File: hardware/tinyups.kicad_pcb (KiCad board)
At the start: 4 copper layers, 150 x 140 mm, 30 parts

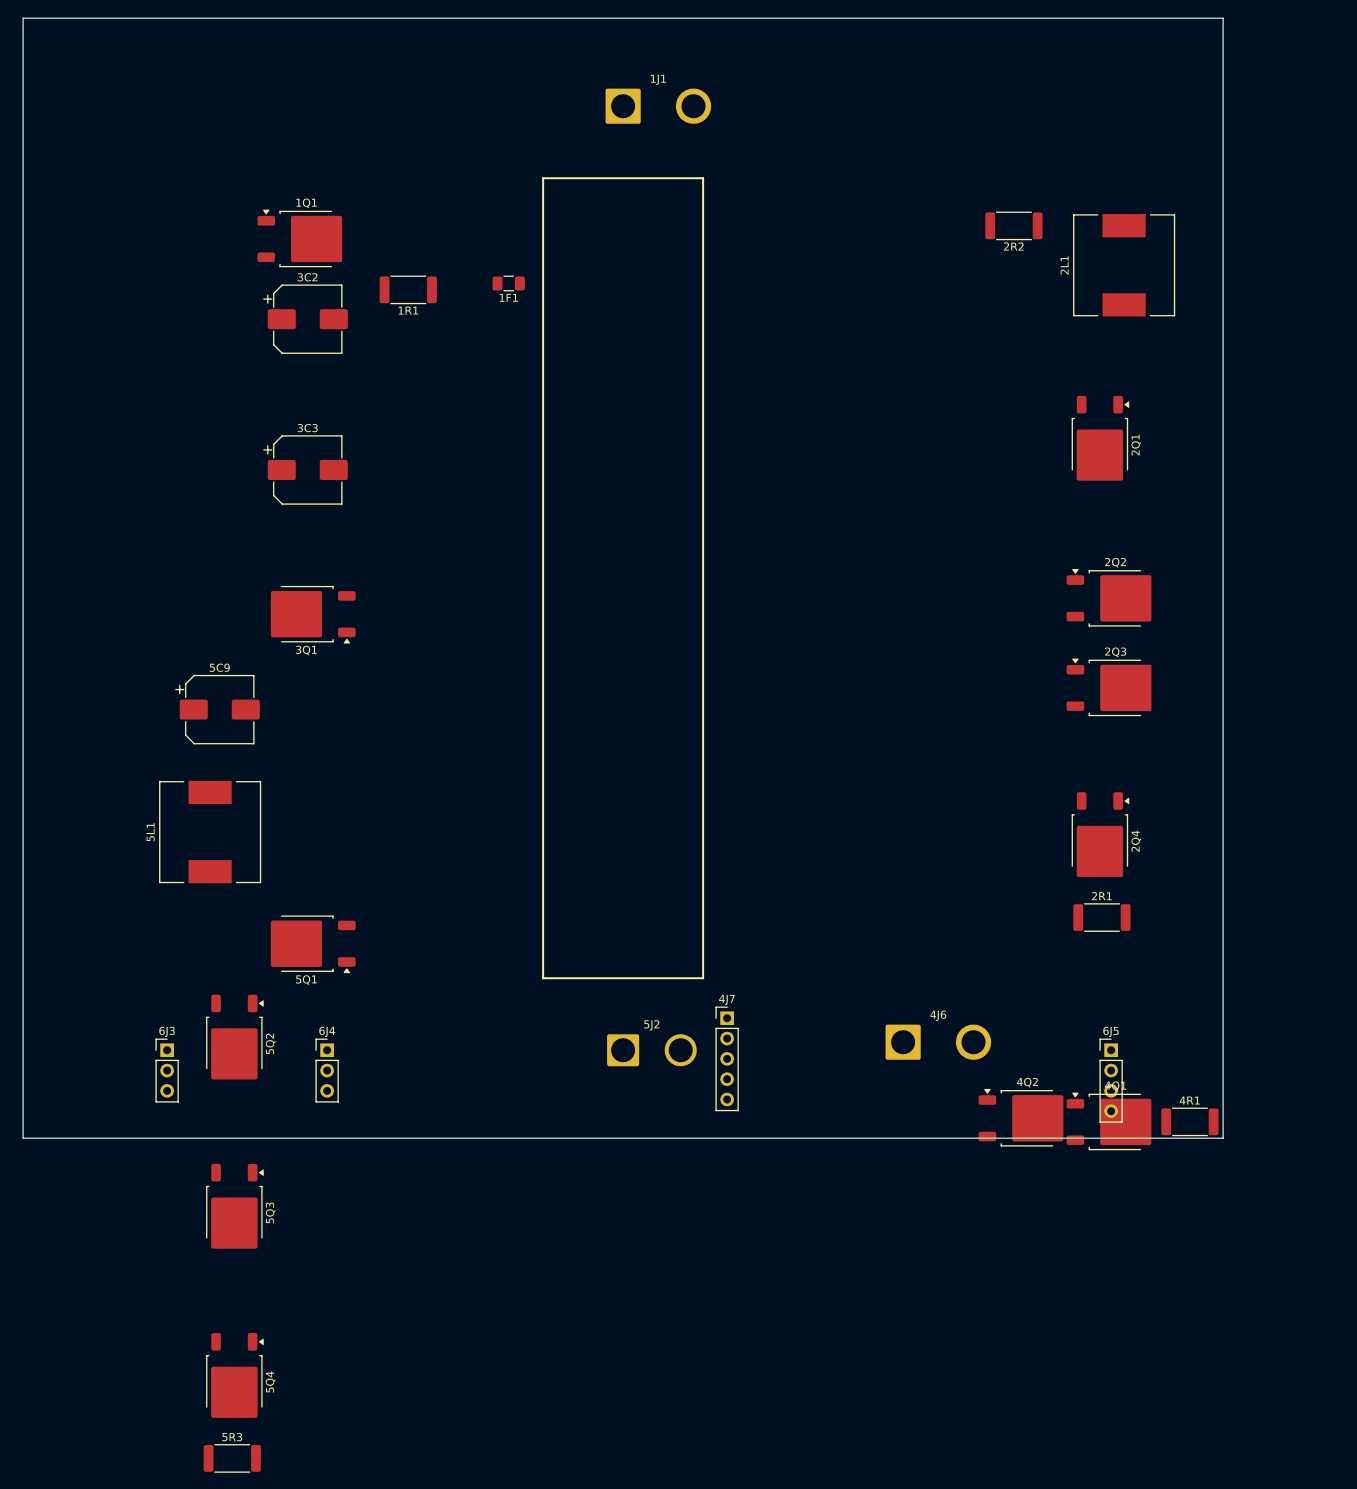
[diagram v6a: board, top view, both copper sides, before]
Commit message: cleanup: adopt placement ui and board 'try5'. archive layout generator and poc
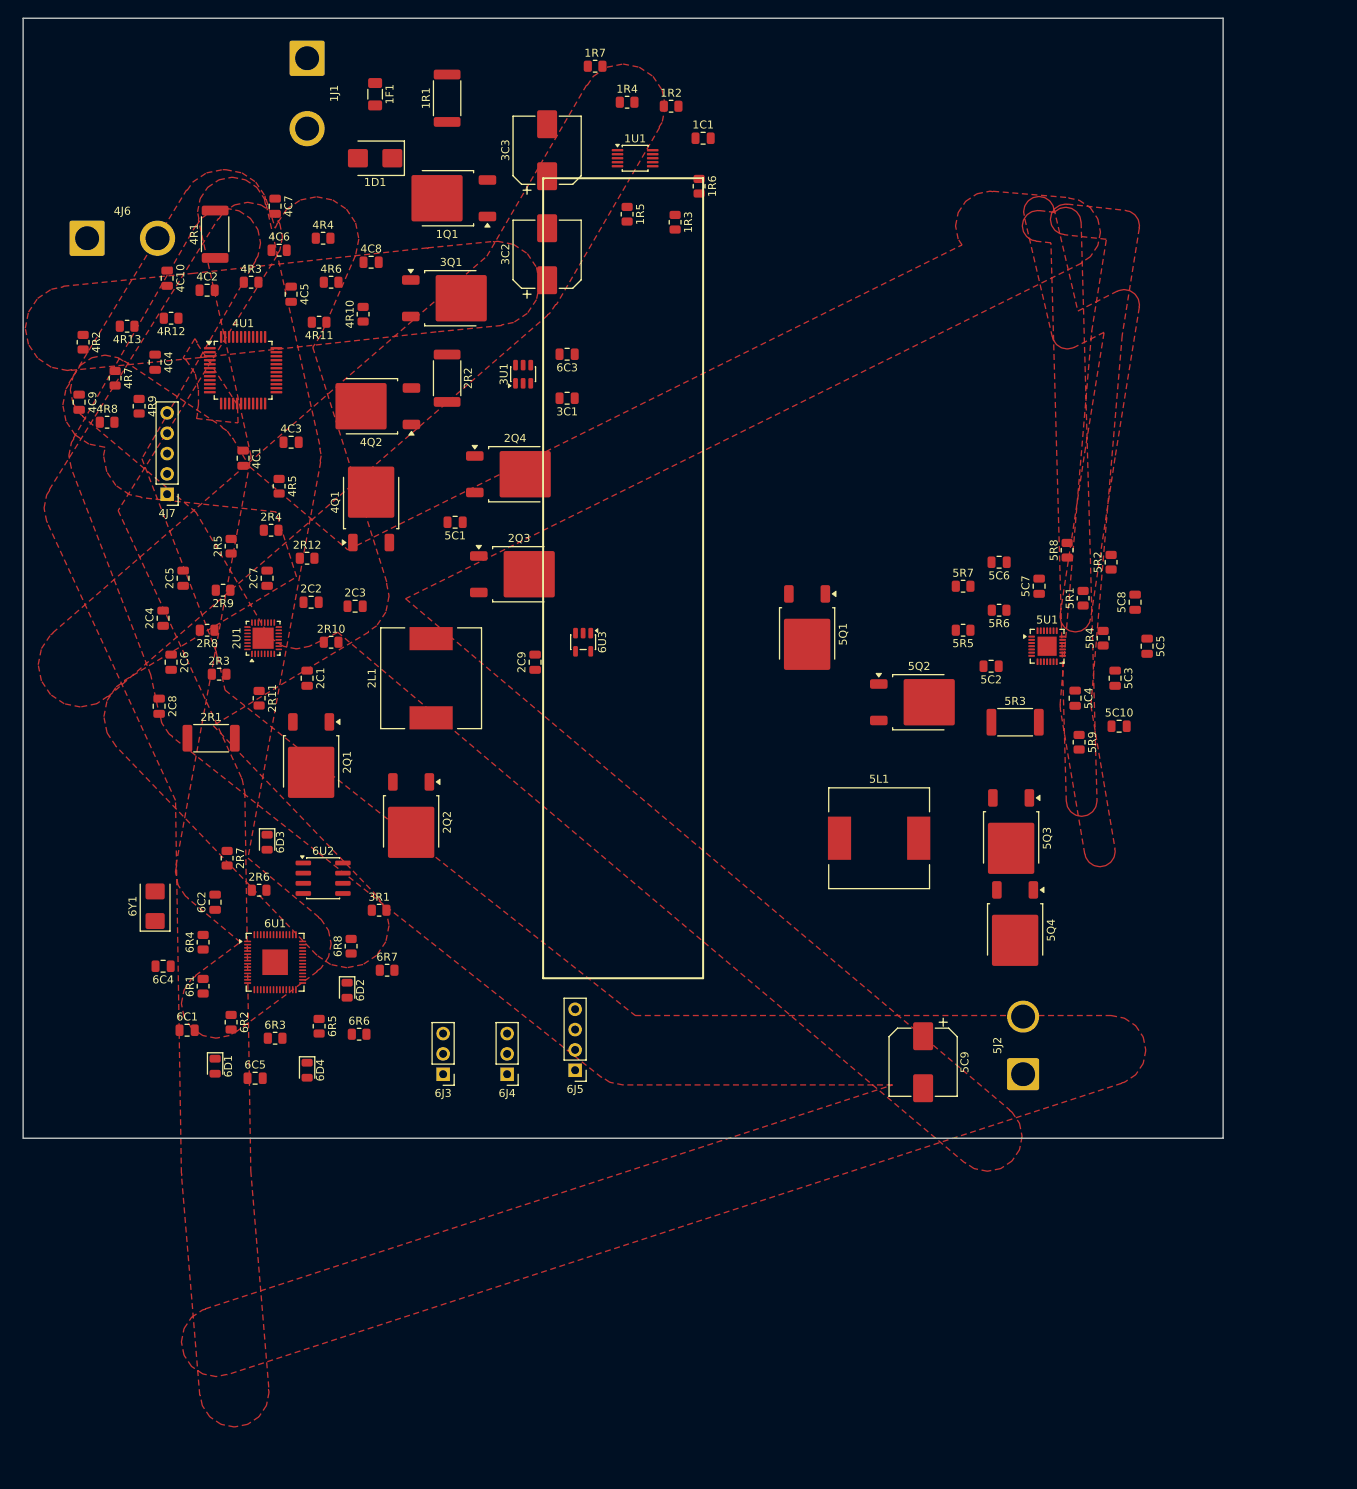
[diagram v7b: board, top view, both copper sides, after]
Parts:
- added 1C1: TBD, Capacitor_SMD:C_0805_2012Metric, F.Cu at (85.0, 15.0)
- added 1D1: SMBJ15A, Diode_SMD:D_SMB, F.Cu at (44.0, 17.5)
- added 1R2: TBD-UV-hi, Resistor_SMD:R_0805_2012Metric, F.Cu at (81.0, 11.0)
- added 1R3: TBD-UV-lo, Resistor_SMD:R_0805_2012Metric, F.Cu at (81.5, 25.5)
- added 1R4: TBD-OV-hi, Resistor_SMD:R_0805_2012Metric, F.Cu at (75.5, 10.5)
- added 1R5: TBD-OV-lo, Resistor_SMD:R_0805_2012Metric, F.Cu at (75.5, 24.5)
- added 1R6: TBD-PWR, Resistor_SMD:R_0805_2012Metric, F.Cu at (84.5, 21.0)
- added 1R7: 100k-PGD, Resistor_SMD:R_0805_2012Metric, F.Cu at (71.5, 6.00)
- added 1U1: LM5069, Package_SO:VSSOP-10_3x3mm_P0.5mm, F.Cu at (76.5, 17.5)
- added 2C1: 47n, Capacitor_SMD:C_0805_2012Metric, F.Cu at (35.5, 82.5)
- added 2C2: 47n, Capacitor_SMD:C_0805_2012Metric, F.Cu at (36.0, 73.0)
- added 2C3: 1u, Capacitor_SMD:C_0805_2012Metric, F.Cu at (41.5, 73.5)
- added 2C4: 1u, Capacitor_SMD:C_0805_2012Metric, F.Cu at (17.5, 75.0)
- added 2C5: 10n, Capacitor_SMD:C_0805_2012Metric, F.Cu at (20.0, 70.0)
- added 2C6: 1n, Capacitor_SMD:C_0805_2012Metric, F.Cu at (18.5, 80.5)
- added 2C7: 100n, Capacitor_SMD:C_0805_2012Metric, F.Cu at (30.5, 70.0)
- added 2C8: 100n, Capacitor_SMD:C_0805_2012Metric, F.Cu at (17.0, 86.0)
- added 2C9: 100n, Capacitor_SMD:C_0805_2012Metric, F.Cu at (64.0, 80.5)
- added 2R10: 10k, Resistor_SMD:R_0805_2012Metric, F.Cu at (38.5, 78.0)
- added 2R11: 10k, Resistor_SMD:R_0805_2012Metric, F.Cu at (29.5, 85.0)
- added 2R12: 10k, Resistor_SMD:R_0805_2012Metric, F.Cu at (35.5, 67.5)
- added 2R3: 100k, Resistor_SMD:R_0805_2012Metric, F.Cu at (24.5, 82.0)
- added 2R4: 100k, Resistor_SMD:R_0805_2012Metric, F.Cu at (31.0, 64.0)
- added 2R5: 10k, Resistor_SMD:R_0805_2012Metric, F.Cu at (26.0, 66.0)
- added 2R6: 10k, Resistor_SMD:R_0805_2012Metric, F.Cu at (29.5, 109.0)
- added 2R7: 10k, Resistor_SMD:R_0805_2012Metric, F.Cu at (25.5, 105.0)
- added 2R8: 10k, Resistor_SMD:R_0805_2012Metric, F.Cu at (23.0, 76.5)
- added 2R9: 10k, Resistor_SMD:R_0805_2012Metric, F.Cu at (25.0, 71.5)
- added 2U1: BQ25720, Package_DFN_QFN:QFN-32-1EP_4x4mm_P0.4mm_EP2.65x2.65mm, F.Cu at (30.0, 77.5)
- added 3C1: 100n, Capacitor_SMD:C_0805_2012Metric, F.Cu at (68.0, 47.5)
- added 3R1: 100k, Resistor_SMD:R_0805_2012Metric, F.Cu at (44.5, 111.5)
- added 3U1: LM74700-Q1, Package_TO_SOT_SMD:SOT-23-6, F.Cu at (62.5, 44.5)
- added 4C1: 1u, Capacitor_SMD:C_0805_2012Metric, F.Cu at (27.5, 55.0)
- added 4C10: 100n, Capacitor_SMD:C_0805_2012Metric, F.Cu at (18.0, 32.5)
- added 4C2: 1u, Capacitor_SMD:C_0805_2012Metric, F.Cu at (23.0, 34.0)
- added 4C3: 1u, Capacitor_SMD:C_0805_2012Metric, F.Cu at (33.5, 53.0)
- added 4C4: 1u, Capacitor_SMD:C_0805_2012Metric, F.Cu at (16.5, 43.0)
- added 4C5: 100n, Capacitor_SMD:C_0805_2012Metric, F.Cu at (33.5, 34.5)
- added 4C6: 100n, Capacitor_SMD:C_0805_2012Metric, F.Cu at (32.0, 29.0)
- added 4C7: 100n, Capacitor_SMD:C_0805_2012Metric, F.Cu at (31.5, 23.5)
- added 4C8: 100n, Capacitor_SMD:C_0805_2012Metric, F.Cu at (43.5, 30.5)
- added 4C9: 100n, Capacitor_SMD:C_0805_2012Metric, F.Cu at (7.00, 48.0)
- added 4R10: 100, Resistor_SMD:R_0805_2012Metric, F.Cu at (42.5, 37.0)
- added 4R11: 100, Resistor_SMD:R_0805_2012Metric, F.Cu at (37.0, 38.0)
- added 4R12: 100, Resistor_SMD:R_0805_2012Metric, F.Cu at (18.5, 37.5)
- added 4R13: 100, Resistor_SMD:R_0805_2012Metric, F.Cu at (13.0, 38.5)
- added 4R2: 10k-NTC, Resistor_SMD:R_0805_2012Metric, F.Cu at (7.50, 40.5)
- added 4R3: 10k-NTC, Resistor_SMD:R_0805_2012Metric, F.Cu at (28.5, 33.0)
- added 4R4: 10k-NTC, Resistor_SMD:R_0805_2012Metric, F.Cu at (37.5, 27.5)
- added 4R5: 100k, Resistor_SMD:R_0805_2012Metric, F.Cu at (32.0, 58.5)
- added 4R6: 100k, Resistor_SMD:R_0805_2012Metric, F.Cu at (38.5, 33.0)
- added 4R7: 100k, Resistor_SMD:R_0805_2012Metric, F.Cu at (11.5, 45.0)
- added 4R8: 100k, Resistor_SMD:R_0805_2012Metric, F.Cu at (10.5, 50.5)
- added 4R9: 100, Resistor_SMD:R_0805_2012Metric, F.Cu at (14.5, 48.5)
- added 4U1: BQ76942, Package_QFP:TQFP-48_7x7mm_P0.5mm, F.Cu at (27.5, 44.0)
- added 5C1: 10u, Capacitor_SMD:C_0805_2012Metric, F.Cu at (54.0, 63.0)
- added 5C10: 10u, Capacitor_SMD:C_0805_2012Metric, F.Cu at (137.0, 88.5)
- added 5C2: 100n, Capacitor_SMD:C_0805_2012Metric, F.Cu at (121.0, 81.0)
- added 5C3: 100n, Capacitor_SMD:C_0805_2012Metric, F.Cu at (136.5, 82.5)
- added 5C4: 10n, Capacitor_SMD:C_0805_2012Metric, F.Cu at (131.5, 85.0)
- added 5C5: 1n, Capacitor_SMD:C_0805_2012Metric, F.Cu at (140.5, 78.5)
- added 5C6: 1n, Capacitor_SMD:C_0805_2012Metric, F.Cu at (122.0, 68.0)
- added 5C7: 1n, Capacitor_SMD:C_0805_2012Metric, F.Cu at (127.0, 71.0)
- added 5C8: 1u, Capacitor_SMD:C_0805_2012Metric, F.Cu at (139.0, 73.0)
- added 5R1: 100k, Resistor_SMD:R_0805_2012Metric, F.Cu at (132.5, 72.5)
- added 5R2: 7k15, Resistor_SMD:R_0805_2012Metric, F.Cu at (136.0, 68.0)
- added 5R4: 27k, Resistor_SMD:R_0805_2012Metric, F.Cu at (135.0, 77.5)
- added 5R5: 93k1, Resistor_SMD:R_0805_2012Metric, F.Cu at (117.5, 76.5)
- added 5R6: 10k, Resistor_SMD:R_0805_2012Metric, F.Cu at (122.0, 74.0)
- added 5R7: 100k, Resistor_SMD:R_0805_2012Metric, F.Cu at (117.5, 71.0)
- added 5R8: 10k, Resistor_SMD:R_0805_2012Metric, F.Cu at (130.5, 66.5)
- added 5R9: 100k, Resistor_SMD:R_0805_2012Metric, F.Cu at (132.0, 90.5)
- added 5U1: LM5176, Package_DFN_QFN:QFN-28-1EP_4x4mm_P0.4mm_EP2.4x2.4mm, F.Cu at (128.0, 78.5)
- added 6C1: 20p, Capacitor_SMD:C_0805_2012Metric, F.Cu at (20.5, 126.5)
- added 6C2: 20p, Capacitor_SMD:C_0805_2012Metric, F.Cu at (24.0, 110.5)
- added 6C3: 10u, Capacitor_SMD:C_0805_2012Metric, F.Cu at (68.0, 42.0)
- added 6C4: 10u, Capacitor_SMD:C_0805_2012Metric, F.Cu at (17.5, 118.5)
- added 6C5: 1u, Capacitor_SMD:C_0805_2012Metric, F.Cu at (29.0, 132.5)
- added 6D1: LED, LED_SMD:LED_0805_2012Metric, F.Cu at (24.0, 131.0)
- added 6D2: LED, LED_SMD:LED_0805_2012Metric, F.Cu at (40.5, 121.5)
- added 6D3: LED, LED_SMD:LED_0805_2012Metric, F.Cu at (30.5, 103.0)
- added 6D4: LED, LED_SMD:LED_0805_2012Metric, F.Cu at (35.5, 131.5)
- added 6R1: 1k, Resistor_SMD:R_0805_2012Metric, F.Cu at (22.5, 121.0)
- added 6R2: 1k, Resistor_SMD:R_0805_2012Metric, F.Cu at (26.0, 125.5)
- added 6R3: 1k, Resistor_SMD:R_0805_2012Metric, F.Cu at (31.5, 127.5)
- added 6R4: 1k, Resistor_SMD:R_0805_2012Metric, F.Cu at (22.5, 115.5)
- added 6R5: 1k, Resistor_SMD:R_0805_2012Metric, F.Cu at (37.0, 126.0)
- added 6R6: 27, Resistor_SMD:R_0805_2012Metric, F.Cu at (42.0, 127.0)
- added 6R7: 27, Resistor_SMD:R_0805_2012Metric, F.Cu at (45.5, 119.0)
- added 6R8: 10k, Resistor_SMD:R_0805_2012Metric, F.Cu at (41.0, 116.0)
- added 6U1: RP2040, Package_DFN_QFN:QFN-56-1EP_7x7mm_P0.4mm_EP3.2x3.2mm, F.Cu at (31.5, 118.0)
- added 6U2: W25Q128, Package_SO:SOIC-8_3.9x4.9mm_P1.27mm, F.Cu at (37.5, 107.5)
- added 6U3: 3V3, Package_TO_SOT_SMD:SOT-23-5, F.Cu at (70.0, 78.0)
- added 6Y1: 12MHz, Crystal:Crystal_SMD_5032-2Pin_5.0x3.2mm, F.Cu at (16.5, 111.0)
- moved 4R1 164.8 mm to (24.0, 27.0), turned to 90 degrees
- moved 4J6 143.2 mm to (8.00, 27.5)
- moved 5R3 134.3 mm to (124.0, 88.0)
- moved 4Q1 121.1 mm to (43.5, 60.5), turned to 90 degrees
- moved 4Q2 121.1 mm to (43.5, 48.5), turned to 180 degrees
- moved 2R1 113.6 mm to (23.5, 90.0)
- moved 5Q4 112.8 mm to (124.0, 114.0)
- moved 5Q3 107.8 mm to (123.5, 102.5)
- moved 2Q1 106.3 mm to (36.0, 93.0)
- moved 2L1 100.8 mm to (51.0, 82.5)
- moved 5C9 98.3 mm to (112.5, 130.5), turned to -90 degrees
- moved 4J7 95.9 mm to (18.0, 59.5), turned to 180 degrees
- moved 5Q2 95.7 mm to (112.0, 85.5), turned to 0 degrees
- moved 2Q2 92.4 mm to (48.5, 100.5), turned to -90 degrees
- moved 2Q4 86.3 mm to (61.5, 57.0), turned to 0 degrees
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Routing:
- added copper zone on F.Cu, net /+12V_IN
- added copper zone on F.Cu, net /N_AF
- added copper zone on F.Cu, net /SW1
- added copper zone on F.Cu, net /SW1_OUT
- added copper zone on F.Cu, net /SW2
- added copper zone on F.Cu, net /SW2_OUT
- added copper zone on F.Cu, net /VBAT
- added copper zone on F.Cu, net /VIN_SYS
- added copper zone on F.Cu, net /VOUT12
- added copper zone on F.Cu, net /VSYS

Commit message: fix placement with new ui features
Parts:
- 1F1: footprint Fuse:Fuse_1206_3216Metric -> Fuse:Fuse_Blade_ATO_directSolder
- 1R1, 2R1, 2R2, 4R1, 5R3: footprint Resistor_SMD:R_2512_6332Metric -> Resistor_SMD:R_Shunt_Vishay_WSR2_WSR3
